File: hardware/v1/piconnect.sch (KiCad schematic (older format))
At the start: 8 parts, among them CON1 BARREL_JACK, P1 CONN_02X05, P11 CONN_02X05, P12 CONN_02X05, P13 CONN_02X05, P5 CONN_02X05, P6 CONN_02X05, U5 Pi2_Connector

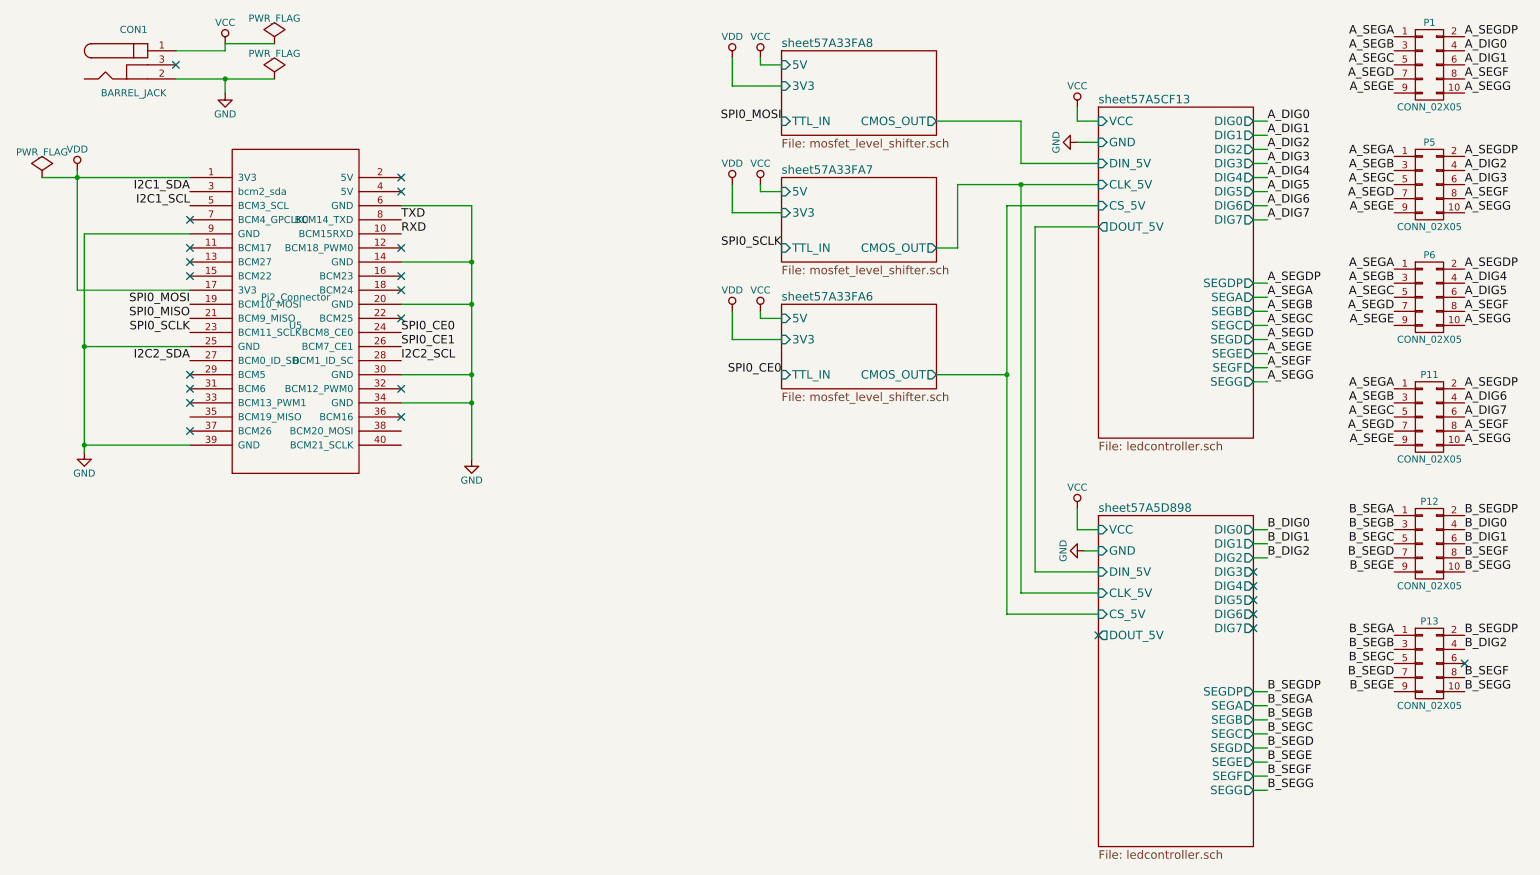
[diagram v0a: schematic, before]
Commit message: Re-arrange switch connector pinout to simpler single-row header. Re-route the switch boards accordingly.
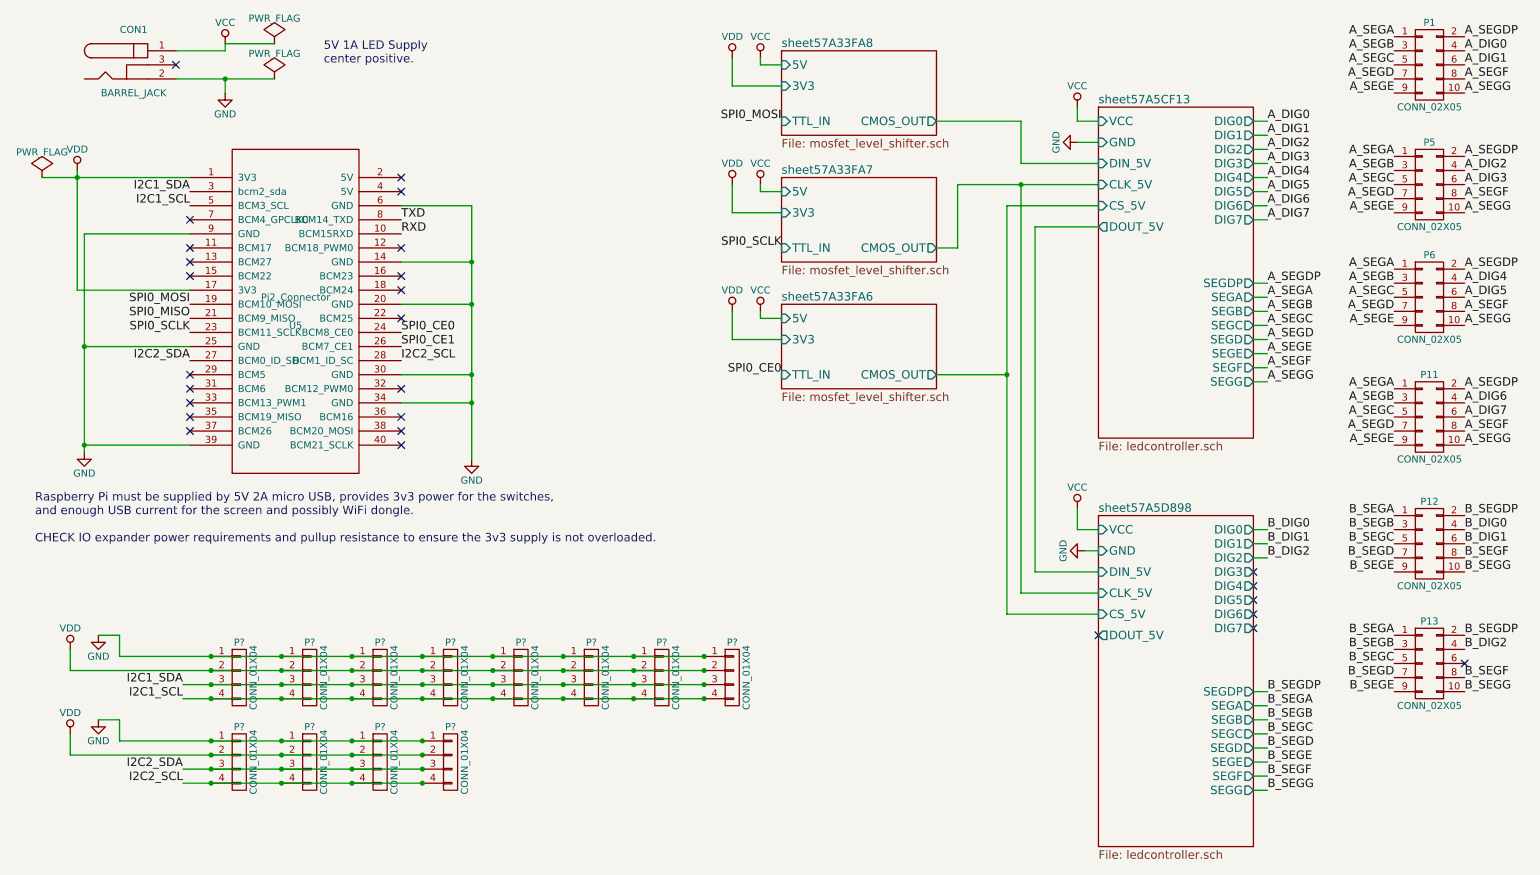
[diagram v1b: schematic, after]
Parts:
- added P? (x12): CONN_01X04, symbol CONN_01X04
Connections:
- net GND: now also P?.1 (P1), P?.1 (P1), P?.1 (P1), P?.1 (P1), P?.1 (P1), P?.1 (P1), P?.1 (P1), P?.1 (P1), P?.1 (P1), P?.1 (P1), P?.1 (P1), P?.1 (P1)
- net I2C1_SCL: now also P?.4 (P4), P?.4 (P4), P?.4 (P4), P?.4 (P4), P?.4 (P4), P?.4 (P4), P?.4 (P4), P?.4 (P4)
- net I2C1_SDA: now also P?.3 (P3), P?.3 (P3), P?.3 (P3), P?.3 (P3), P?.3 (P3), P?.3 (P3), P?.3 (P3), P?.3 (P3)
- net I2C2_SCL: now also P?.4 (P4), P?.4 (P4), P?.4 (P4), P?.4 (P4)
- net I2C2_SDA: now also P?.3 (P3), P?.3 (P3), P?.3 (P3), P?.3 (P3)
- net VDD: now also P?.2 (P2), P?.2 (P2), P?.2 (P2), P?.2 (P2), P?.2 (P2), P?.2 (P2), P?.2 (P2), P?.2 (P2), P?.2 (P2), P?.2 (P2), P?.2 (P2), P?.2 (P2)
- no-connect marks 24 -> 27
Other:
- note added: "5V 1A LED Supply\ncenter positive."
- note added: "Raspberry Pi must be supplied by 5V 2A micro USB, provides 3v3 power for the switches,\nand enough USB current for the screen and possibly WiFi dongle.\n\nCHECK IO expander power requirements and pullup resistance to ensure the 3v3 supply is not overloaded.\n"

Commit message: Add new schematics for additional switch boards
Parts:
- P1, P10, P11, P12, P2, P3, P4, P5, P6, P7, P8, P9: renamed from P?; footprint (none) -> Pin_Headers:Pin_Header_Straight_1x04
- P13: renamed from P1; footprint Pin_Headers:Pin_Header_Angled_2x05 -> Pin_Headers:Pin_Header_Straight_2x05
- P14: renamed from P5; footprint Pin_Headers:Pin_Header_Angled_2x05 -> Pin_Headers:Pin_Header_Straight_2x05
- P15: renamed from P6; footprint Pin_Headers:Pin_Header_Angled_2x05 -> Pin_Headers:Pin_Header_Straight_2x05
- P16: renamed from P11; footprint Pin_Headers:Pin_Header_Angled_2x05 -> Pin_Headers:Pin_Header_Straight_2x05
- P17: renamed from P12; footprint Pin_Headers:Pin_Header_Angled_2x05 -> Pin_Headers:Pin_Header_Straight_2x05
- P18: renamed from P13; footprint Pin_Headers:Pin_Header_Angled_2x05 -> Pin_Headers:Pin_Header_Straight_2x05
- U1: renamed from U5; footprint MODULE -> Pin_Headers:Pin_Header_Straight_2x20
